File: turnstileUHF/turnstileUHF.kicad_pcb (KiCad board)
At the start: 2 copper layers, 98 x 98 mm, 32 parts

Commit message: Moved one hole
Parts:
- moved H3 1.02 mm to (79.5, 3.20)
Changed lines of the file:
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@@
 	(footprint "inspireFly:MountingHole_2mm_custom"
 		(layer "F.Cu")
-		(at 80.49 3.2)
+		(at 79.47 3.2)
 		(descr "Mounting Hole 2.2mm, M2, generated by kicad-footprint-generator mountinghole.py")
 		(tags "mountinghole M2 ISO7380")

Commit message: Test burn resistors placed
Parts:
- added REF**: R_2512_6332Metric_Pad1.40x3.35mm_HandSolder, Resistor_SMD:R_2512_6332Metric_Pad1.40x3.35mm_HandSolder, F.Cu at (161.8, 89.0)
- added REF**: R_2512_6332Metric_Pad1.40x3.35mm_HandSolder, Resistor_SMD:R_2512_6332Metric_Pad1.40x3.35mm_HandSolder, F.Cu at (213.6, 141.1)
- added REF**: R_2512_6332Metric_Pad1.40x3.35mm_HandSolder, Resistor_SMD:R_2512_6332Metric_Pad1.40x3.35mm_HandSolder, F.Cu at (155.9, 94.7)
- added REF**: R_2512_6332Metric_Pad1.40x3.35mm_HandSolder, Resistor_SMD:R_2512_6332Metric_Pad1.40x3.35mm_HandSolder, F.Cu at (207.7, 146.7)
- added REF**: R_2512_6332Metric_Pad1.40x3.35mm_HandSolder, Resistor_SMD:R_2512_6332Metric_Pad1.40x3.35mm_HandSolder, F.Cu at (210.7, 143.9)
- added REF**: R_2512_6332Metric_Pad1.40x3.35mm_HandSolder, Resistor_SMD:R_2512_6332Metric_Pad1.40x3.35mm_HandSolder, F.Cu at (204.8, 149.7)
- added REF**: R_2512_6332Metric_Pad1.40x3.35mm_HandSolder, Resistor_SMD:R_2512_6332Metric_Pad1.40x3.35mm_HandSolder, F.Cu at (153.1, 97.6)
- added REF**: R_2512_6332Metric_Pad1.40x3.35mm_HandSolder, Resistor_SMD:R_2512_6332Metric_Pad1.40x3.35mm_HandSolder, F.Cu at (158.9, 91.8)
- moved H13 151.7 mm to (196.8, 99.2)
- moved H15 151.7 mm to (220.8, 101.2)
- moved H16 151.7 mm to (203.8, 106.2)
- moved H17 151.7 mm to (162.8, 133.2)
- moved H18 151.7 mm to (145.8, 138.2)
- moved H19 151.7 mm to (137.5, 138.7)
- moved H21 151.7 mm to (137.5, 150.2)
- moved H22 151.7 mm to (169.8, 140.2)
- moved H23 151.7 mm to (164.8, 157.2)
- moved H29 151.7 mm to (229.1, 150.2)
- moved H7 151.7 mm to (137.5, 89.2)
- moved H8 151.7 mm to (137.5, 95.0)
- moved H9 151.7 mm to (168.3, 89.0)
- moved H1 151.7 mm to (152.8, 73.9)
- moved H10 151.7 mm to (229.1, 89.2)
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
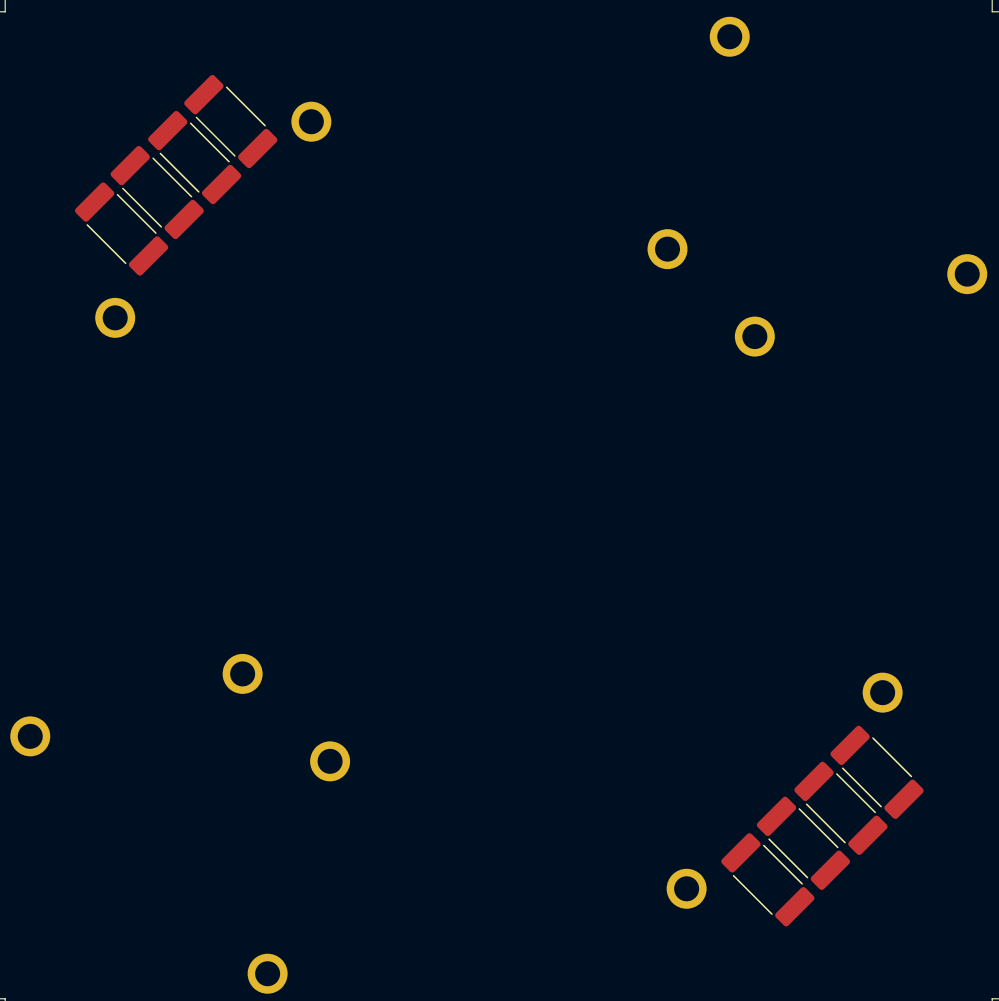
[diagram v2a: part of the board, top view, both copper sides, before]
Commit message: burn wire routing
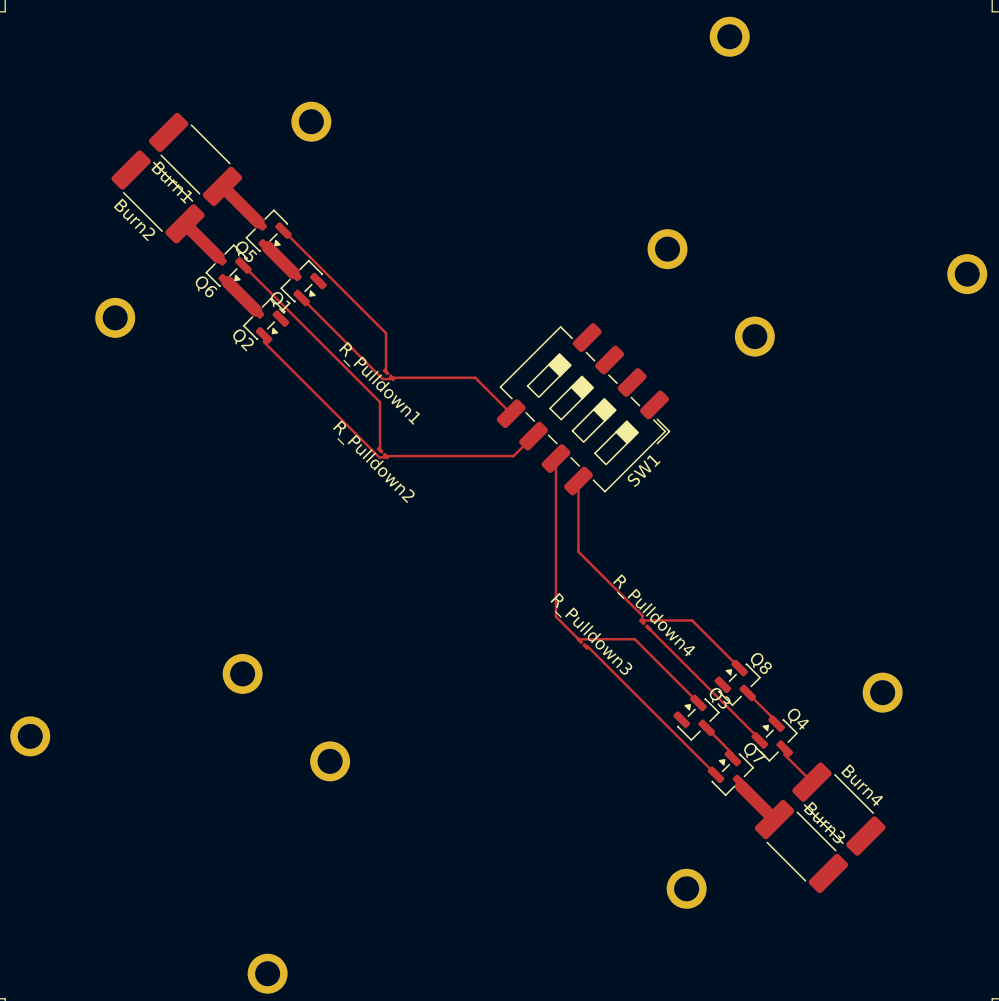
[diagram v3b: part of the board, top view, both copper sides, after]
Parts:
- removed REF** (x8): R_2512_6332Metric_Pad1.40x3.35mm_HandSolder, Resistor_SMD:R_2512_6332Metric_Pad1.40x3.35mm_HandSolder
- added Burn1: 10, Resistor_SMD:R_2512_6332Metric_Pad1.40x3.35mm_HandSolder, F.Cu at (159.0, 92.0)
- added Burn2: 10, Resistor_SMD:R_2512_6332Metric_Pad1.40x3.35mm_HandSolder, F.Cu at (156.0, 95.0)
- added Burn3: 10, Resistor_SMD:R_2512_6332Metric_Pad1.40x3.35mm_HandSolder, F.Cu at (207.5, 147.0)
- added Burn4: 10, Resistor_SMD:R_2512_6332Metric_Pad1.40x3.35mm_HandSolder, F.Cu at (210.5, 144.0)
- added Q1: 2N7002, Package_TO_SOT_SMD:SOT-23, F.Cu at (167.5, 101.8)
- added Q2: 2N7002, Package_TO_SOT_SMD:SOT-23, F.Cu at (164.5, 104.8)
- added Q3: 2N7002, Package_TO_SOT_SMD:SOT-23, F.Cu at (199.2, 136.8)
- added Q4: 2N7002, Package_TO_SOT_SMD:SOT-23, F.Cu at (205.5, 138.5)
- added Q5: AO3401A, Package_TO_SOT_SMD:SOT-23, F.Cu at (164.7, 97.7)
- added Q6: AO3401A, Package_TO_SOT_SMD:SOT-23, F.Cu at (161.5, 100.5)
- added Q7: AO3401A, Package_TO_SOT_SMD:SOT-23, F.Cu at (202.0, 141.2)
- added Q8: 2N7002, Package_TO_SOT_SMD:SOT-23, F.Cu at (202.5, 134.0)
- added R_Pulldown1: 10k, Resistor_SMD:R_01005_0402Metric_Pad0.57x0.30mm_HandSolder, F.Cu at (174.5, 109.2)
- added R_Pulldown2: 10k, Resistor_SMD:R_01005_0402Metric_Pad0.57x0.30mm_HandSolder, F.Cu at (174.0, 115.5)
- added R_Pulldown3: 10k, Resistor_SMD:R_01005_0402Metric_Pad0.57x0.30mm_HandSolder, F.Cu at (190.0, 130.8)
- added R_Pulldown4: 10k, Resistor_SMD:R_01005_0402Metric_Pad0.57x0.30mm_HandSolder, F.Cu at (195.0, 129.2)
- added SW1: SW_DIP_x04, Button_Switch_SMD:SW_DIP_SPSTx04_Slide_6.7x11.72mm_W8.61mm_P2.54mm_LowProfile, F.Cu at (190.0, 112.0)
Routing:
- net Net-(Q3-G): track 0.00 -> 27.0 mm
- net Net-(Q2-G): track 0.00 -> 26.6 mm
- net Net-(Q8-G): track 0.00 -> 22.8 mm
- net Net-(Q1-G): track 0.00 -> 20.7 mm
- net Net-(Q6-S): track 0.00 -> 19.3 mm
- net Net-(Q5-S): track 0.00 -> 14.7 mm
- net Net-(Q7-S): track 0.00 -> 14.7 mm
- net Net-(Q4-S): track 0.00 -> 12.7 mm
- net Net-(Q5-D): track 0.00 -> 4.08 mm
- net Net-(Q7-D): track 0.00 -> 4.04 mm
- net Net-(Q6-D): track 0.00 -> 3.79 mm
- net Net-(Q4-D): track 0.00 -> 3.58 mm
- net Net-(Q4-G): track 0.00 -> 3.41 mm
- net Net-(Q3-D): track 0.00 -> 3.28 mm
- net Net-(Q2-D): track 0.00 -> 3.28 mm
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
